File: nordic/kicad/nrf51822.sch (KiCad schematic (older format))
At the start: 17 parts, among them P1 CONN_01X04, P3 CONN_01X01, SW1 SW_Push, U1 BALF-NRF01E3, X1 Crystal

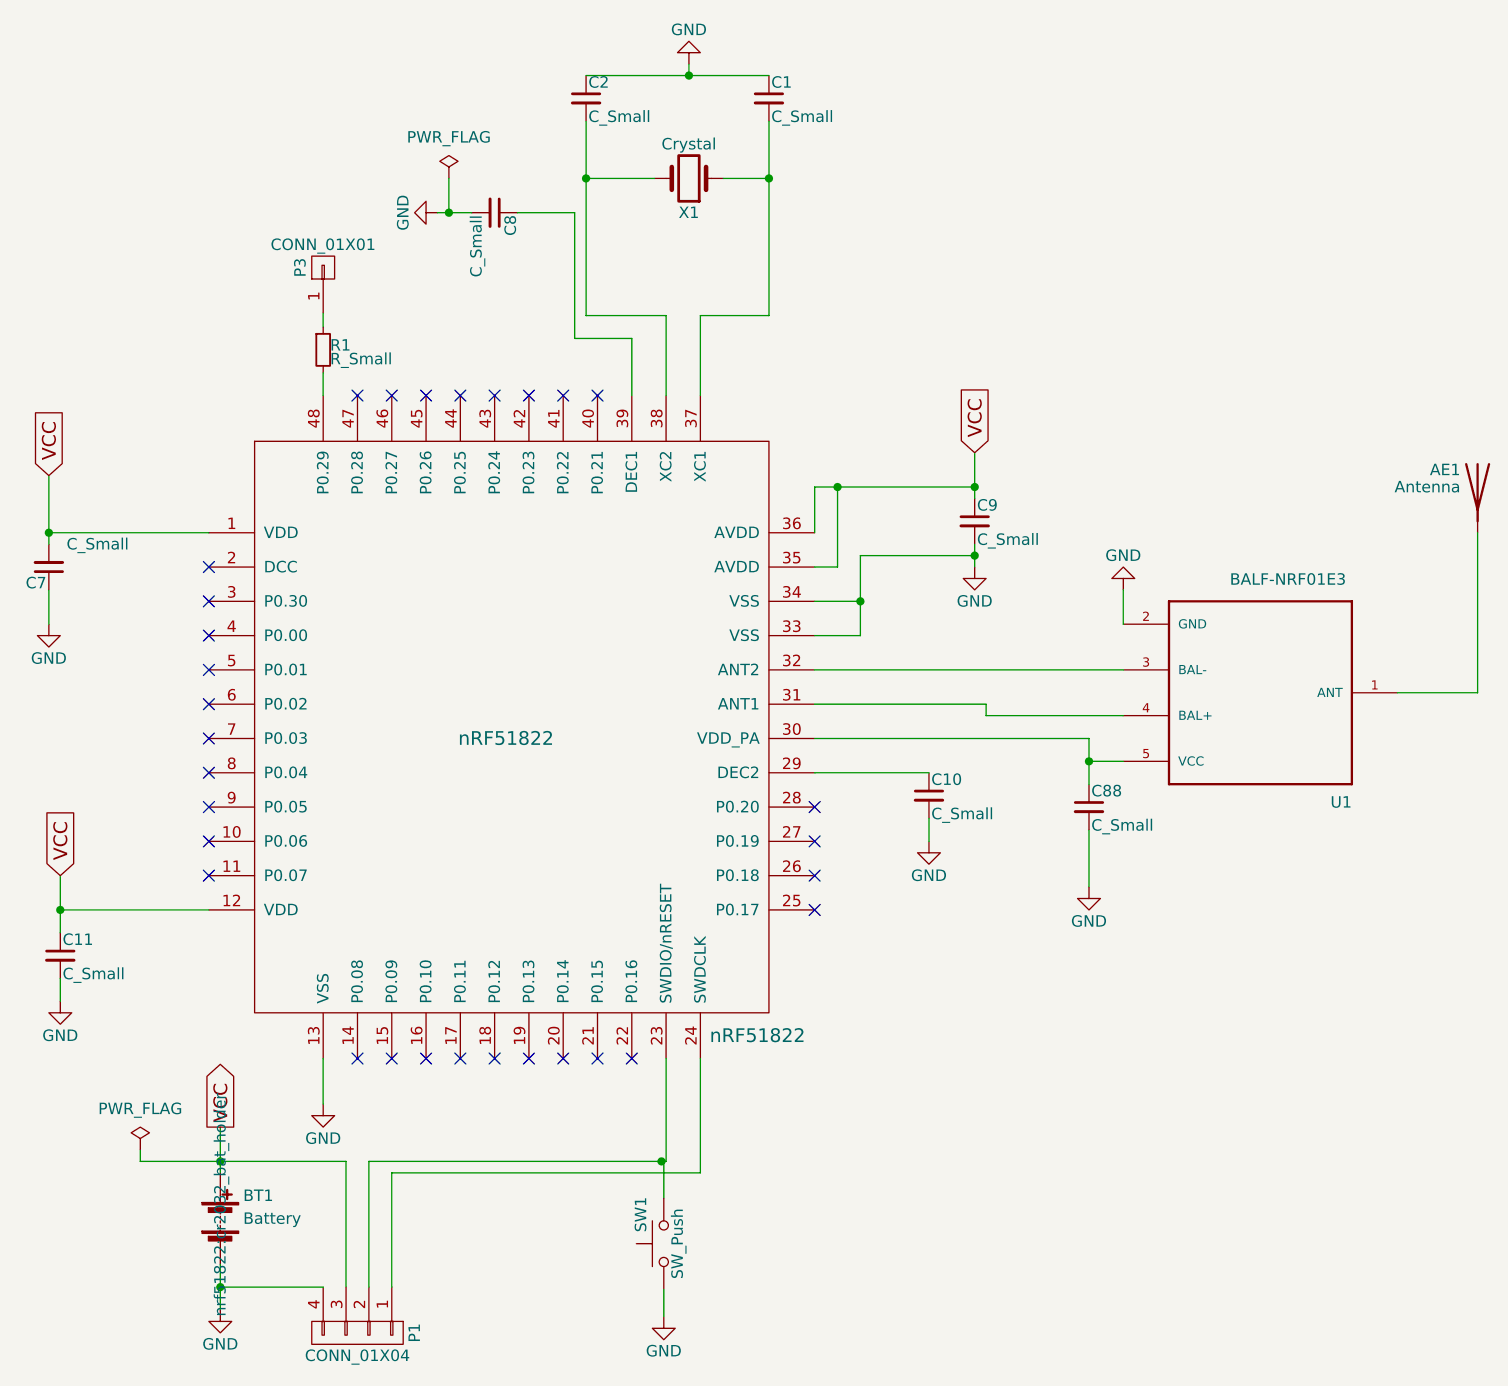
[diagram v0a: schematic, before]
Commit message: Adicionado componentes 3d no diretório, aumentado a logo e colocado led para teste POST no lugar do botão de reset
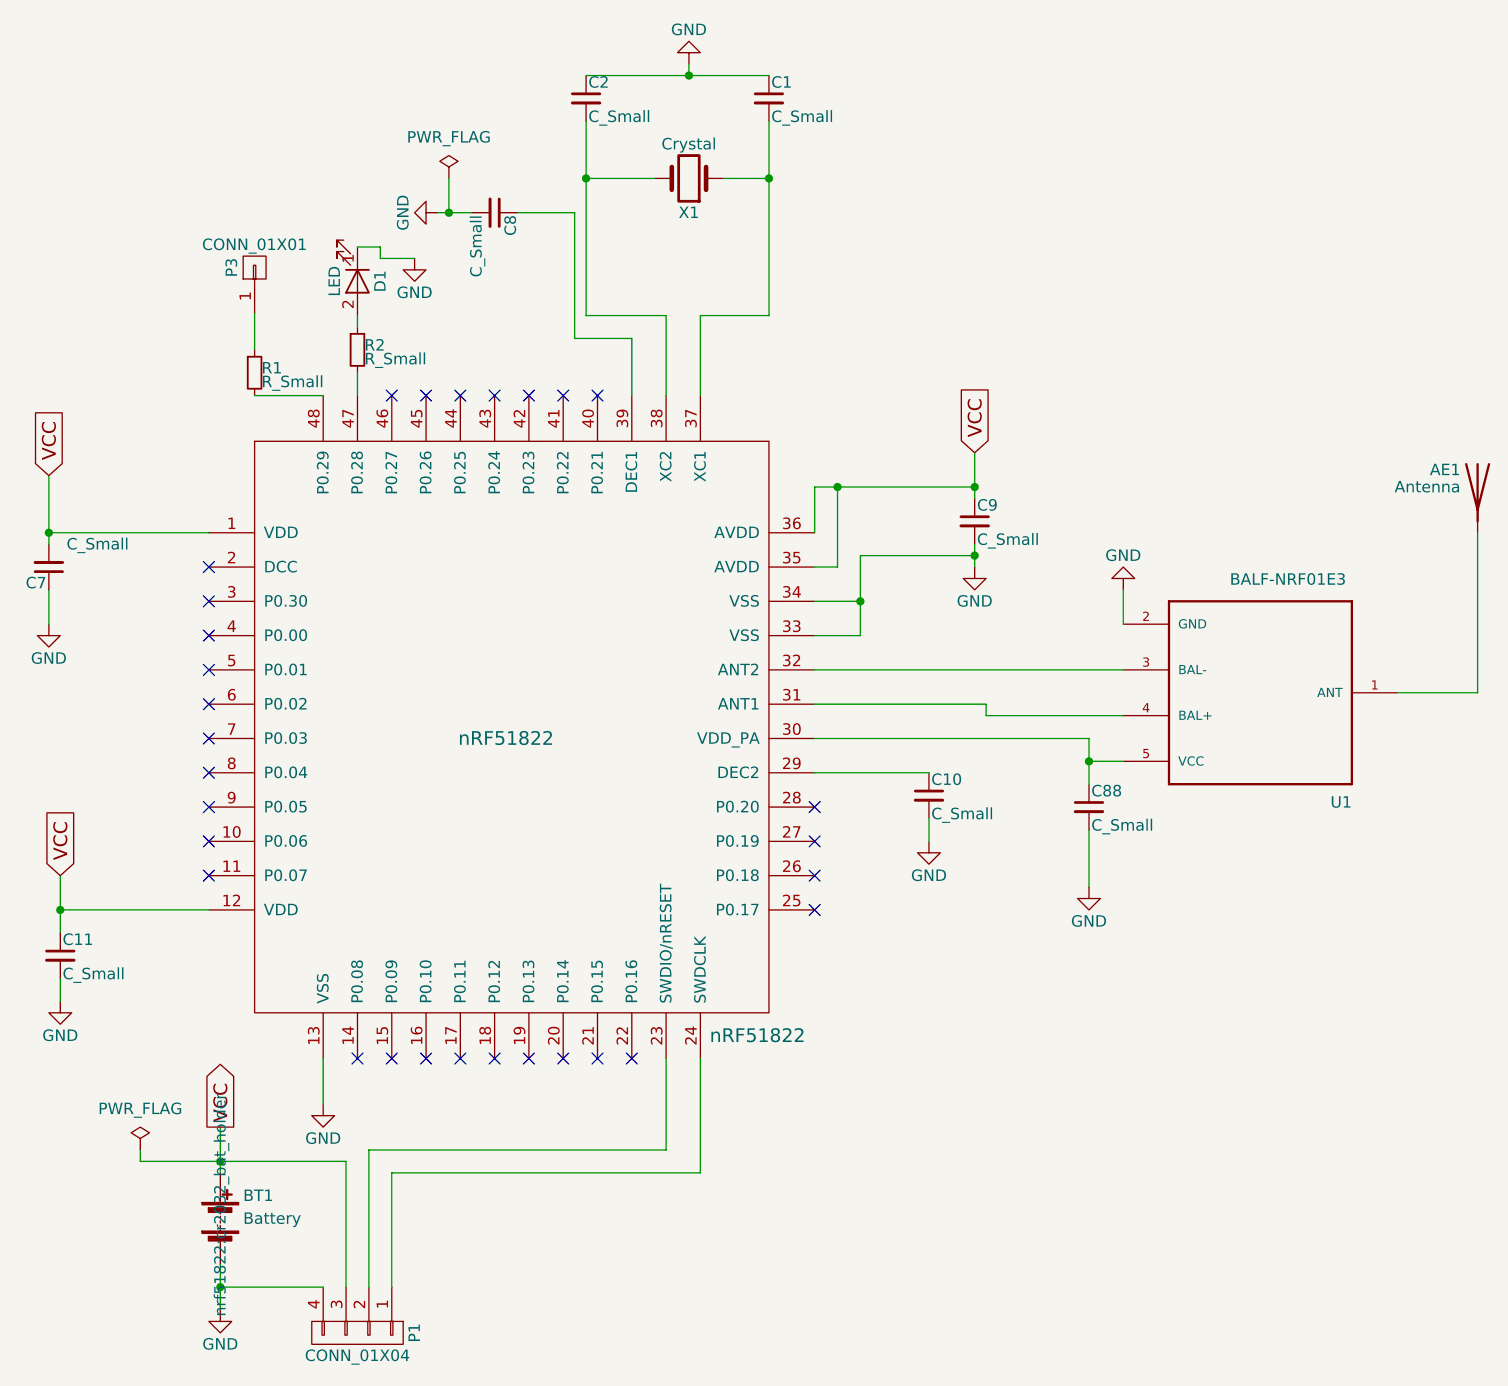
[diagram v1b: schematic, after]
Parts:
- removed SW1: SW_Push, Buttons_Switches_SMD:SW_SPST_TL3342, symbol SW_Push
- added D1: LED, LEDs:LED_0805, symbol LED
- added R2: R_Small, Resistors_SMD:R_0402, symbol R_Small
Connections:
- net GND: now also D1.1 (K)
- net at nRF51822.47 (P0.28): now also R2.2
- new net: D1.2 (A), R2.1
- no-connect marks 31 -> 30
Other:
- moved on the sheet: P3, R1
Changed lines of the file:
@@
 	1    0    0    -1
 $EndComp
-NoConn ~ 5000 2350
 NoConn ~ 5150 2350
 NoConn ~ 5450 2350
@@
 	4400 5550 4400 5750
 Wire Wire Line
-	6350 5700 6350 5250
-Wire Wire Line
-	5050 5700 6350 5700
-Wire Wire Line
 	6500 5750 5150 5750
 Wire Wire Line
@@
 	4950 5700 4950 6250
 Wire Wire Line
-	5050 5700 5050 6250
+	5050 5650 5050 6250
 Wire Wire Line
 	5150 5750 5150 6250
@@
 	9900 3650 9550 3650
 $Comp
-L SW_Push SW1
-U 1 1 59399148
-P 6340 6060
-F 0 "SW1" H 6390 6160 50  0000 L CNN
-F 1 "SW_Push" H 6340 6000 50  0000 C CNN
-F 2 "Buttons_Switches_SMD:SW_SPST_TL3342" H 6340 6260 50  0001 C CNN
-F 3 "" H 6340 6260 50  0000 C CNN
-	1    6340 6060
-	0    -1   -1   0
-$EndComp
-Wire Wire Line
-	6340 5860 6340 5700
-Wire Wire Line
-	6340 5700 6330 5700
-Connection ~ 6330 5700
-$Comp
-L GND #PWR013
-U 1 1 593992D9
-P 6340 6380
-F 0 "#PWR013" H 6340 6130 50  0001 C CNN
-F 1 "GND" H 6340 6230 50  0000 C CNN
-F 2 "" H 6340 6380 50  0000 C CNN
-F 3 "" H 6340 6380 50  0000 C CNN
-	1    6340 6380
-	1    0    0    -1
-$EndComp
-Wire Wire Line
-	6340 6380 6340 6260
-$Comp
 L nRF51822 nRF51822
 U 1 1 5926221C
@@
 L R_Small R1
 U 1 1 5939CCF8
-P 4850 2150
-F 0 "R1" H 4880 2170 50  0000 L CNN
-F 1 "R_Small" H 4880 2110 50  0000 L CNN
-F 2 "Resistors_SMD:R_0402" H 4850 2150 50  0001 C CNN
-F 3 "" H 4850 2150 50  0000 C CNN
-	1    4850 2150
-	1    0    0    -1
-$EndComp
-Wire Wire Line
-	4850 2350 4850 2250
+P 4550 2250
+F 0 "R1" H 4580 2270 50  0000 L CNN
+F 1 "R_Small" H 4580 2210 50  0000 L CNN
+F 2 "Resistors_SMD:R_0402" H 4550 2250 50  0001 C CNN
+F 3 "" H 4550 2250 50  0000 C CNN
+	1    4550 2250
+	1    0    0    -1
+$EndComp
+Wire Wire Line
+	4850 2350 4550 2350
 $Comp
 L CONN_01X01 P3
 U 1 1 5939DBBE
-P 4850 1790
-F 0 "P3" H 4850 1890 50  0000 C CNN
-F 1 "CONN_01X01" V 4950 1790 50  0000 C CNN
-F 2 "Pin_Headers:Pin_Header_Straight_1x01_Pitch2.00mm" H 4850 1790 50  0001 C CNN
-F 3 "" H 4850 1790 50  0000 C CNN
-	1    4850 1790
+P 4550 1790
+F 0 "P3" H 4550 1890 50  0000 C CNN
+F 1 "CONN_01X01" V 4650 1790 50  0000 C CNN
+F 2 "Pin_Headers:Pin_Header_Straight_1x01_Pitch2.00mm" H 4550 1790 50  0001 C CNN
+F 3 "" H 4550 1790 50  0000 C CNN
+	1    4550 1790
 	0    -1   -1   0
 $EndComp
 Wire Wire Line
-	4850 2050 4850 1990
+	4550 2150 4550 1990
 Wire Wire Line
 	3700 4600 4350 4600
+Wire Wire Line
+	6350 5250 6350 5650
+Wire Wire Line
+	6350 5650 5050 5650
+$Comp
+L R_Small R2
+U 1 1 5966DC34
+P 5000 2150
+F 0 "R2" H 5030 2170 50  0000 L CNN
+F 1 "R_Small" H 5030 2110 50  0000 L CNN
+F 2 "Resistors_SMD:R_0402" H 5000 2150 50  0001 C CNN
+F 3 "" H 5000 2150 50  0000 C CNN
+	1    5000 2150
+	1    0    0    -1
+$EndComp
+$Comp
+L LED D1
+U 1 1 5966DC85
+P 5000 1850
+F 0 "D1" H 5000 1950 50  0000 C CNN
+F 1 "LED" H 5000 1750 50  0000 C CNN
+F 2 "LEDs:LED_0805" H 5000 1850 50  0001 C CNN
+F 3 "" H 5000 1850 50  0001 C CNN
+	1    5000 1850
+	0    1    1    0
+$EndComp
+Wire Wire Line
+	5000 2350 5000 2250
+Wire Wire Line
+	5000 2050 5000 2000
+$Comp
+L GND #PWR013
+U 1 1 5966DE59
+P 5250 1750
+F 0 "#PWR013" H 5250 1500 50  0001 C CNN
+F 1 "GND" H 5250 1600 50  0000 C CNN
+F 2 "" H 5250 1750 50  0001 C CNN
+F 3 "" H 5250 1750 50  0001 C CNN
+	1    5250 1750
+	1    0    0    -1
+$EndComp
+Wire Wire Line
+	5250 1750 5100 1750
+Wire Wire Line
+	5100 1750 5100 1700
+Wire Wire Line
+	5100 1700 5000 1700
 $EndSCHEMATC
